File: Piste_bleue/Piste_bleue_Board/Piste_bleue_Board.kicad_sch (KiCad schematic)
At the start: 24 parts, among them J1 Conn_01x08_Female, J2 Conn_01x04_Female_Grove, Q1 2N2222, SW1 SW_Push_Dual, U1 ESP32-DEVKITC-32D, U2 gas_sens, U3 LTC1050ACN8#PBF

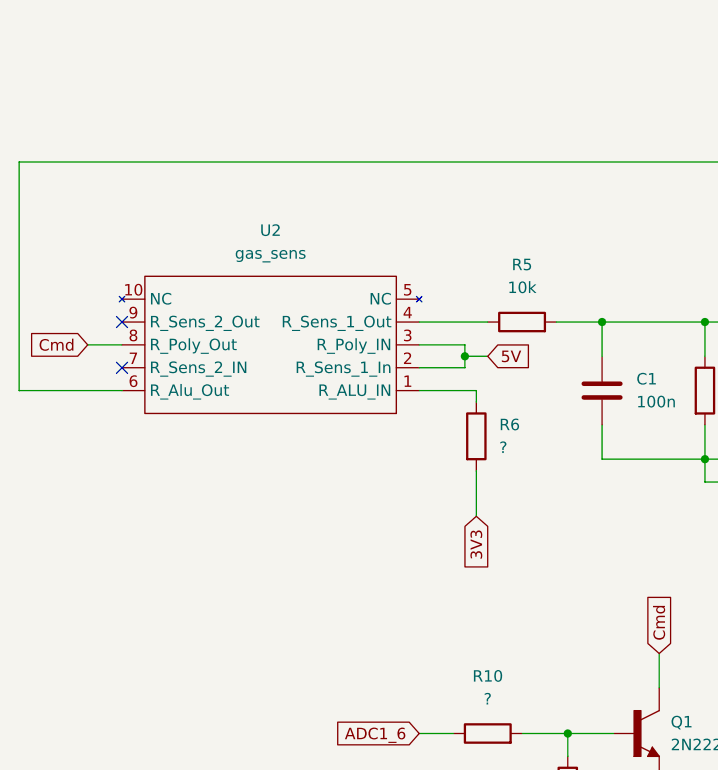
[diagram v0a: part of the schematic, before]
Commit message: Nettoyage des dossiers Ajout du code qui aurait été utilisé avec la board et le capteur produit durant la semaine AIME
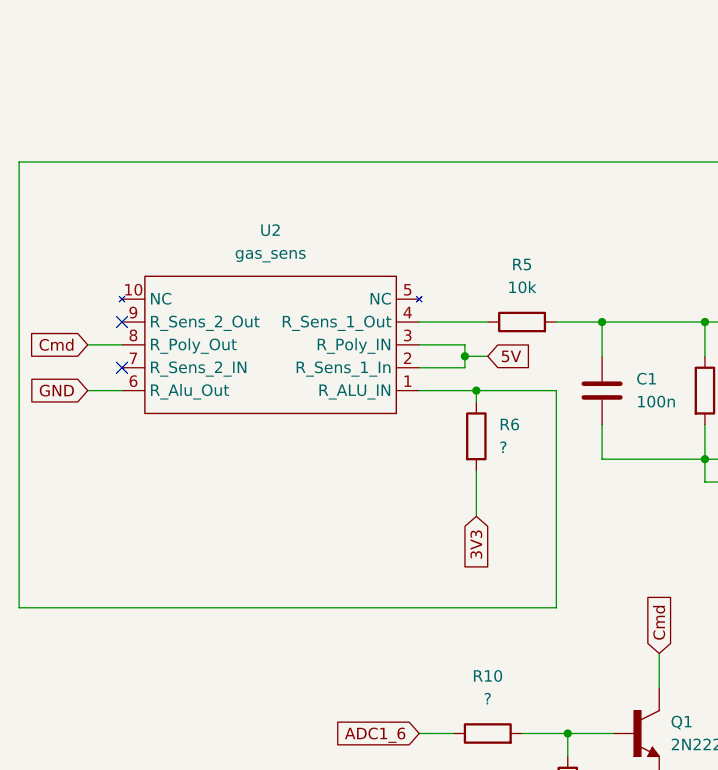
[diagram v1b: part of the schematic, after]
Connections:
- net GND: now also U2.6 (R_Alu_Out)
- net at U1.2 (SENSOR_VP): now also R6.1, U2.1 (R_ALU_IN); no longer U2.6 (R_Alu_Out)
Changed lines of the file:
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@@
   (junction (at 185.42 64.77) (diameter 0) (color 0 0 0 0)
+  )
+  (junction (at 64.77 57.15) (diameter 0) (color 0 0 0 0)
   )
   (junction (at 90.17 64.77) (diameter 0) (color 0 0 0 0)
@@
     (stroke (width 0) (type default) (color 0 0 0 0))
   )
-  (wire (pts (xy 13.97 57.15) (xy 13.97 31.75))
+  (wire (pts (xy 13.97 31.75) (xy 13.97 81.28))
     (stroke (width 0) (type default) (color 0 0 0 0))
   )
@@
     (stroke (width 0) (type default) (color 0 0 0 0))
   )
-  (wire (pts (xy 25.4 57.15) (xy 13.97 57.15))
-    (stroke (width 0) (type default) (color 0 0 0 0))
-  )
   (wire (pts (xy 201.93 64.77) (xy 185.42 64.77))
     (stroke (width 0) (type default) (color 0 0 0 0))
@@
     (stroke (width 0) (type default) (color 0 0 0 0))
   )
+  (wire (pts (xy 73.66 57.15) (xy 73.66 81.28))
+    (stroke (width 0) (type default) (color 0 0 0 0))
+  )
   (wire (pts (xy 74.93 105.41) (xy 74.93 107.95))
     (stroke (width 0) (type default) (color 0 0 0 0))
@@
     (stroke (width 0) (type default) (color 0 0 0 0))
   )
+  (wire (pts (xy 64.77 57.15) (xy 73.66 57.15))
+    (stroke (width 0) (type default) (color 0 0 0 0))
+  )
   (wire (pts (xy 163.83 49.53) (xy 167.64 49.53))
     (stroke (width 0) (type default) (color 0 0 0 0))
@@
     (stroke (width 0) (type default) (color 0 0 0 0))
   )
+  (wire (pts (xy 13.97 81.28) (xy 73.66 81.28))
+    (stroke (width 0) (type default) (color 0 0 0 0))
+  )
   (wire (pts (xy 193.04 81.28) (xy 193.04 69.85))
     (stroke (width 0) (type default) (color 0 0 0 0))
@@
   )
   (wire (pts (xy 179.07 53.34) (xy 179.07 49.53))
+    (stroke (width 0) (type default) (color 0 0 0 0))
+  )
+  (wire (pts (xy 21.59 57.15) (xy 25.4 57.15))
     (stroke (width 0) (type default) (color 0 0 0 0))
   )
@@
       (effects (font (size 1.27 1.27)) (justify right) hide)
     )
+  )
+  (global_label "GND" (shape input) (at 21.59 57.15 180) (fields_autoplaced)
+    (effects (font (size 1.27 1.27)) (justify right))
+    (property "Intersheet References" "${INTERSHEET_REFS}" (id 0) (at 15.1159 57.0706 0)
+      (effects (font (size 1.27 1.27)) (justify right) hide)
+    )
